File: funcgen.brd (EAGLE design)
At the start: 55.4 x 50.2 mm, 71 parts, among them IC1 AD9833, IC4 LM318D, IC5 LM318D, Q2 ASFL1, Q3 16MHz, U1 TLV1117-33IDCY, U2 MICROCHIP_ATMEGA328PB-AUMICRO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, U3 TLV61048DBVR

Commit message: Re-upload board and schematic
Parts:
- moved POT1K 0.76 mm to (51.6, 6.60)
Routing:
- net N$25: track 21.9 -> 22.7 mm
- net -12V: track 67.2 -> 67.7 mm

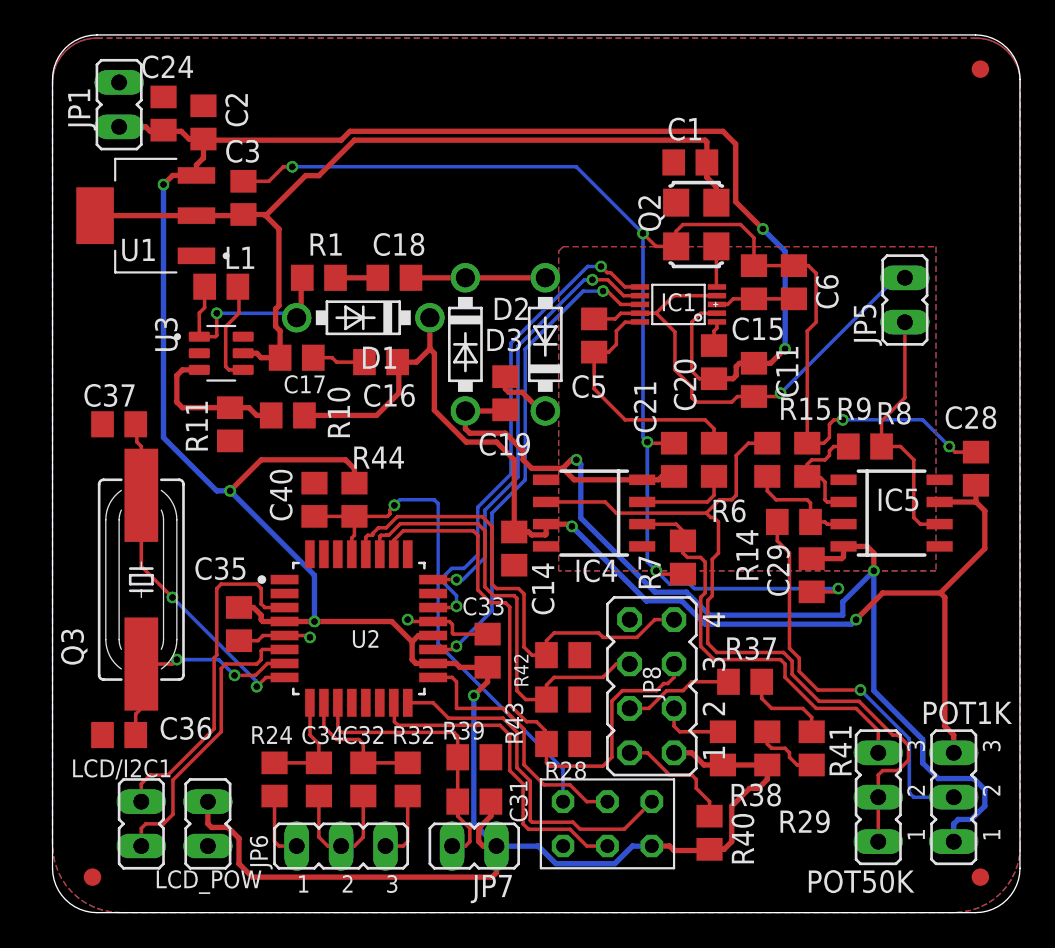
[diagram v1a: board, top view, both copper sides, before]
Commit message: Updated Board and Schematic
Updated Board and Schematic with SMA Schottky diodes and ISP pin 1 marking
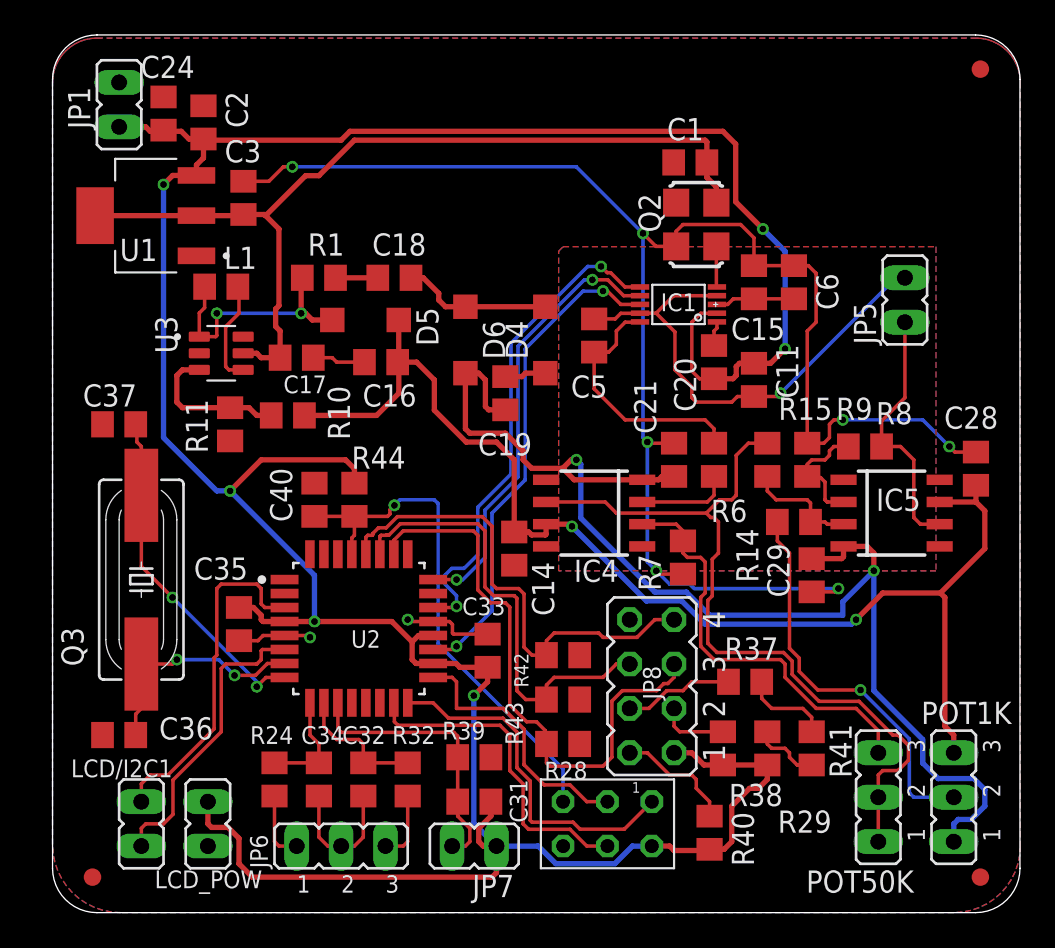
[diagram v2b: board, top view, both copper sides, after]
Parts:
- removed D1, D2, D3: 1N5817-B, diode:DO41-7.6
- added D4, D5, D6: MBR0520LT, diode:SOD123
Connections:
- net +12V: now also D5.C; no longer D1.C
- net -12V: now also D6.A; no longer D2.A
- net N$11: now also D4.A, D6.C; no longer D2.C, D3.A
- net N$12: now also D4.C; no longer D3.C
- net N$9: now also D5.A; no longer D1.A
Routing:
- net -12V: track 67.7 -> 71.6 mm
- net N$9: track 12.4 -> 14.1 mm, vias 1 -> 2
- net N$12: track 3.51 -> 2.37 mm
- net N$11: track 7.69 -> 8.60 mm
- net +12V: track 72.3 -> 71.4 mm
